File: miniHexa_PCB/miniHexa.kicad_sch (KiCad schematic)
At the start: 20 parts, among them SW1 SW_Push, U1 STM32F401RETx, Y2 25mhz

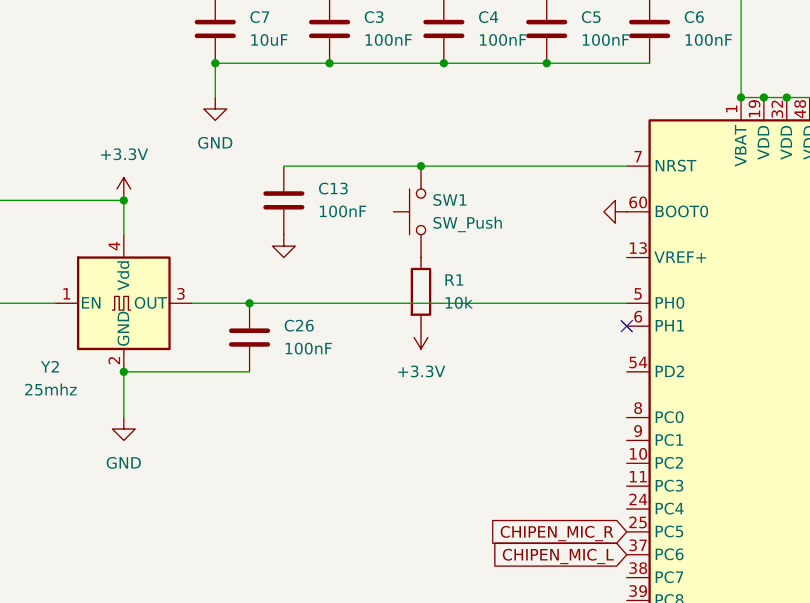
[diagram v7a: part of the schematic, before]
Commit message: added water marks
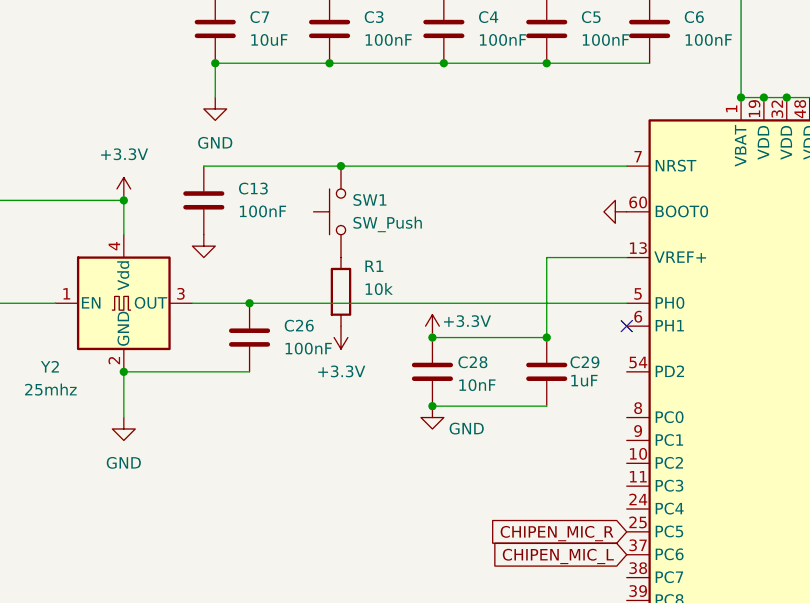
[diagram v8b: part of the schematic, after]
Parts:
- added C28: 10nF, Capacitor_SMD:C_0402_1005Metric, symbol Device:C
- added C29: 1uF, Capacitor_SMD:C_0402_1005Metric, symbol Device:C
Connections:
- net +3.3V: now also U1.13 (VREF+), C28.1, C29.1
- net GND: now also C28.2, C29.2
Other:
- moved on the sheet: C13, R1, SW1
